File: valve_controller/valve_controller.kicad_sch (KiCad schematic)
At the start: 35 parts, among them J1 643260100604, J10 643260100604, J11 643260100604, J2 T4143512051-000, J3 M12A-04PMMP-SF8001, J4 ESP_PROG, J5 643260100604, J6 643260100604, J7 643260100604, J8 643260100604, J9 643260100604, U1 LAN8720A, U2 ADS1115IDGS, U3 MCP4728, U4 ESP32-WROOM-32, U5 LM2596S-5, U7 ADS1115IDGS, U8 MCP4728, U9 AP2112K-3.3, Y2 ASE-25.000MHZ-LC-T

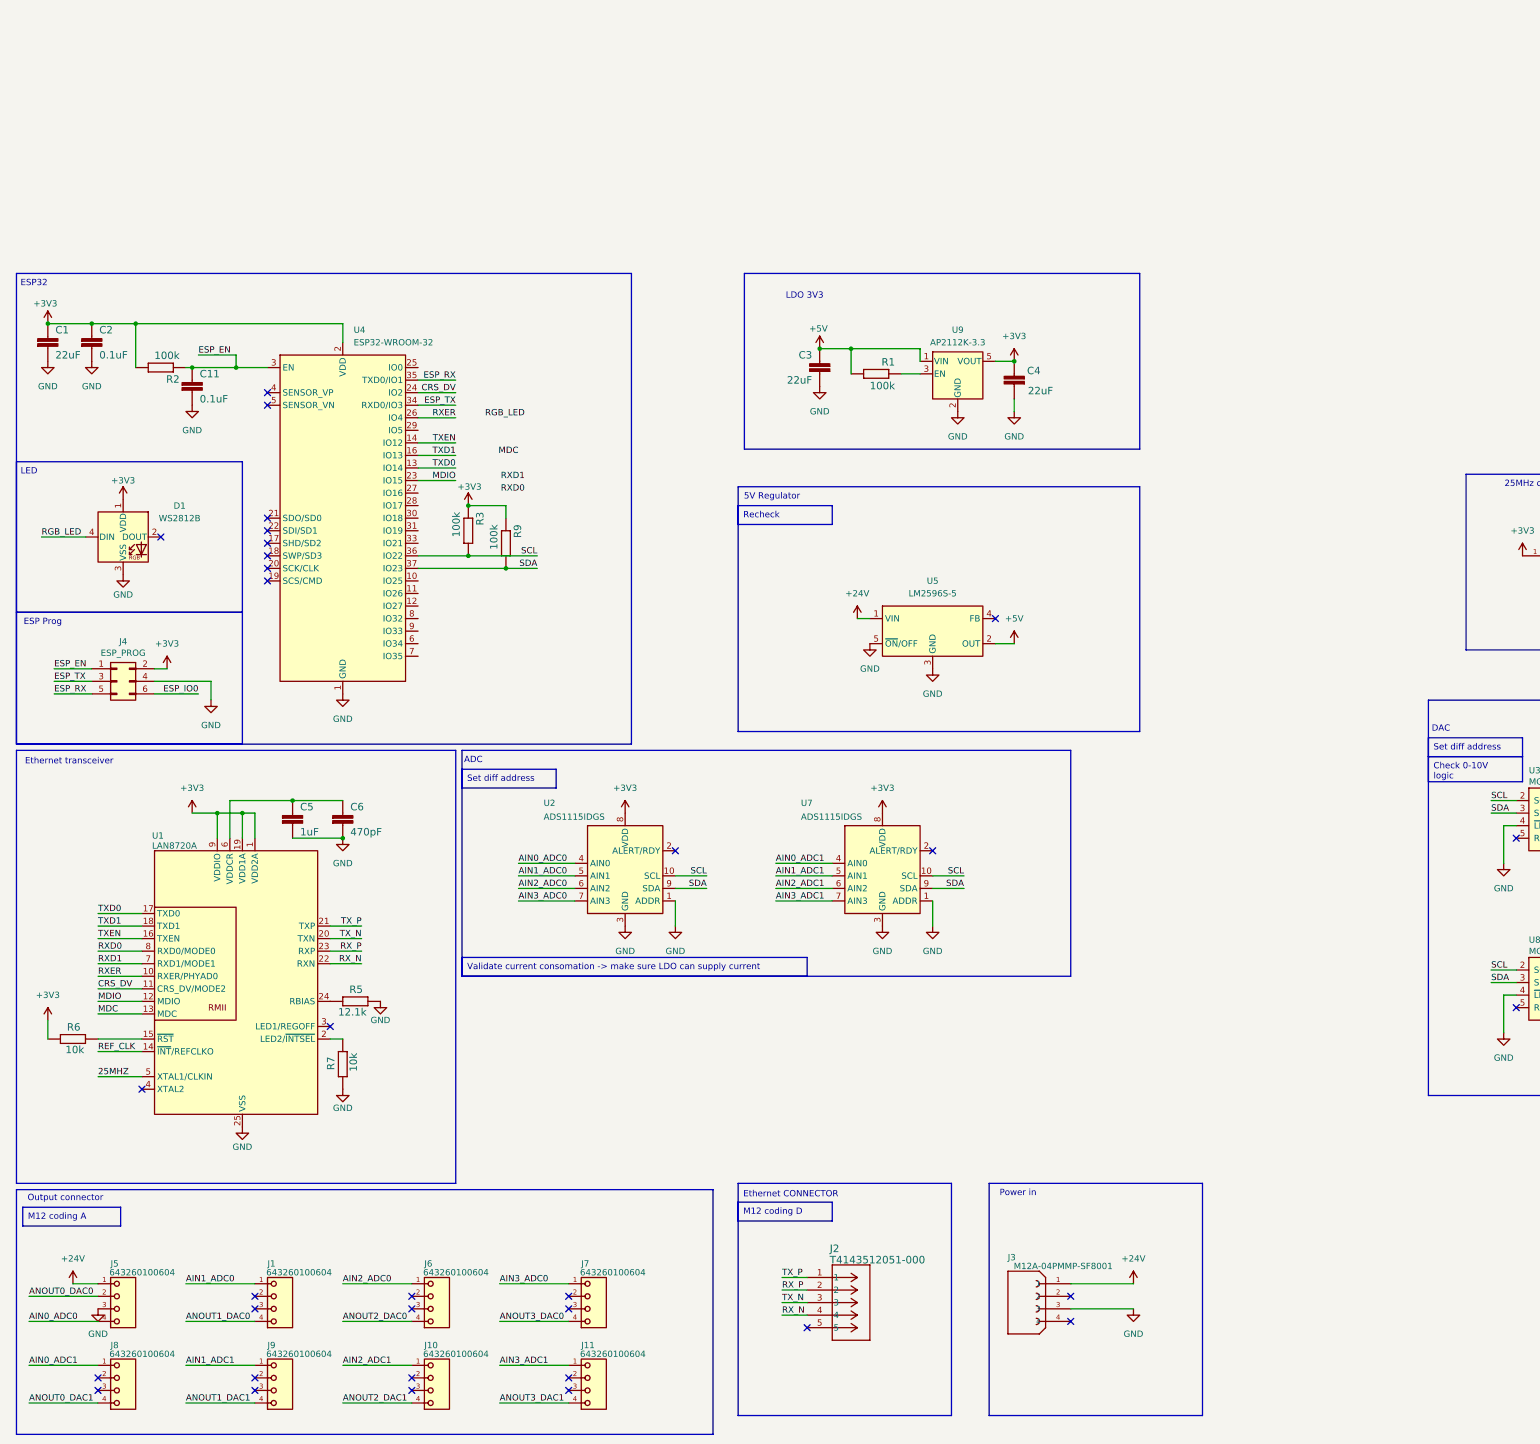
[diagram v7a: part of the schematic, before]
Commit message: new regulator
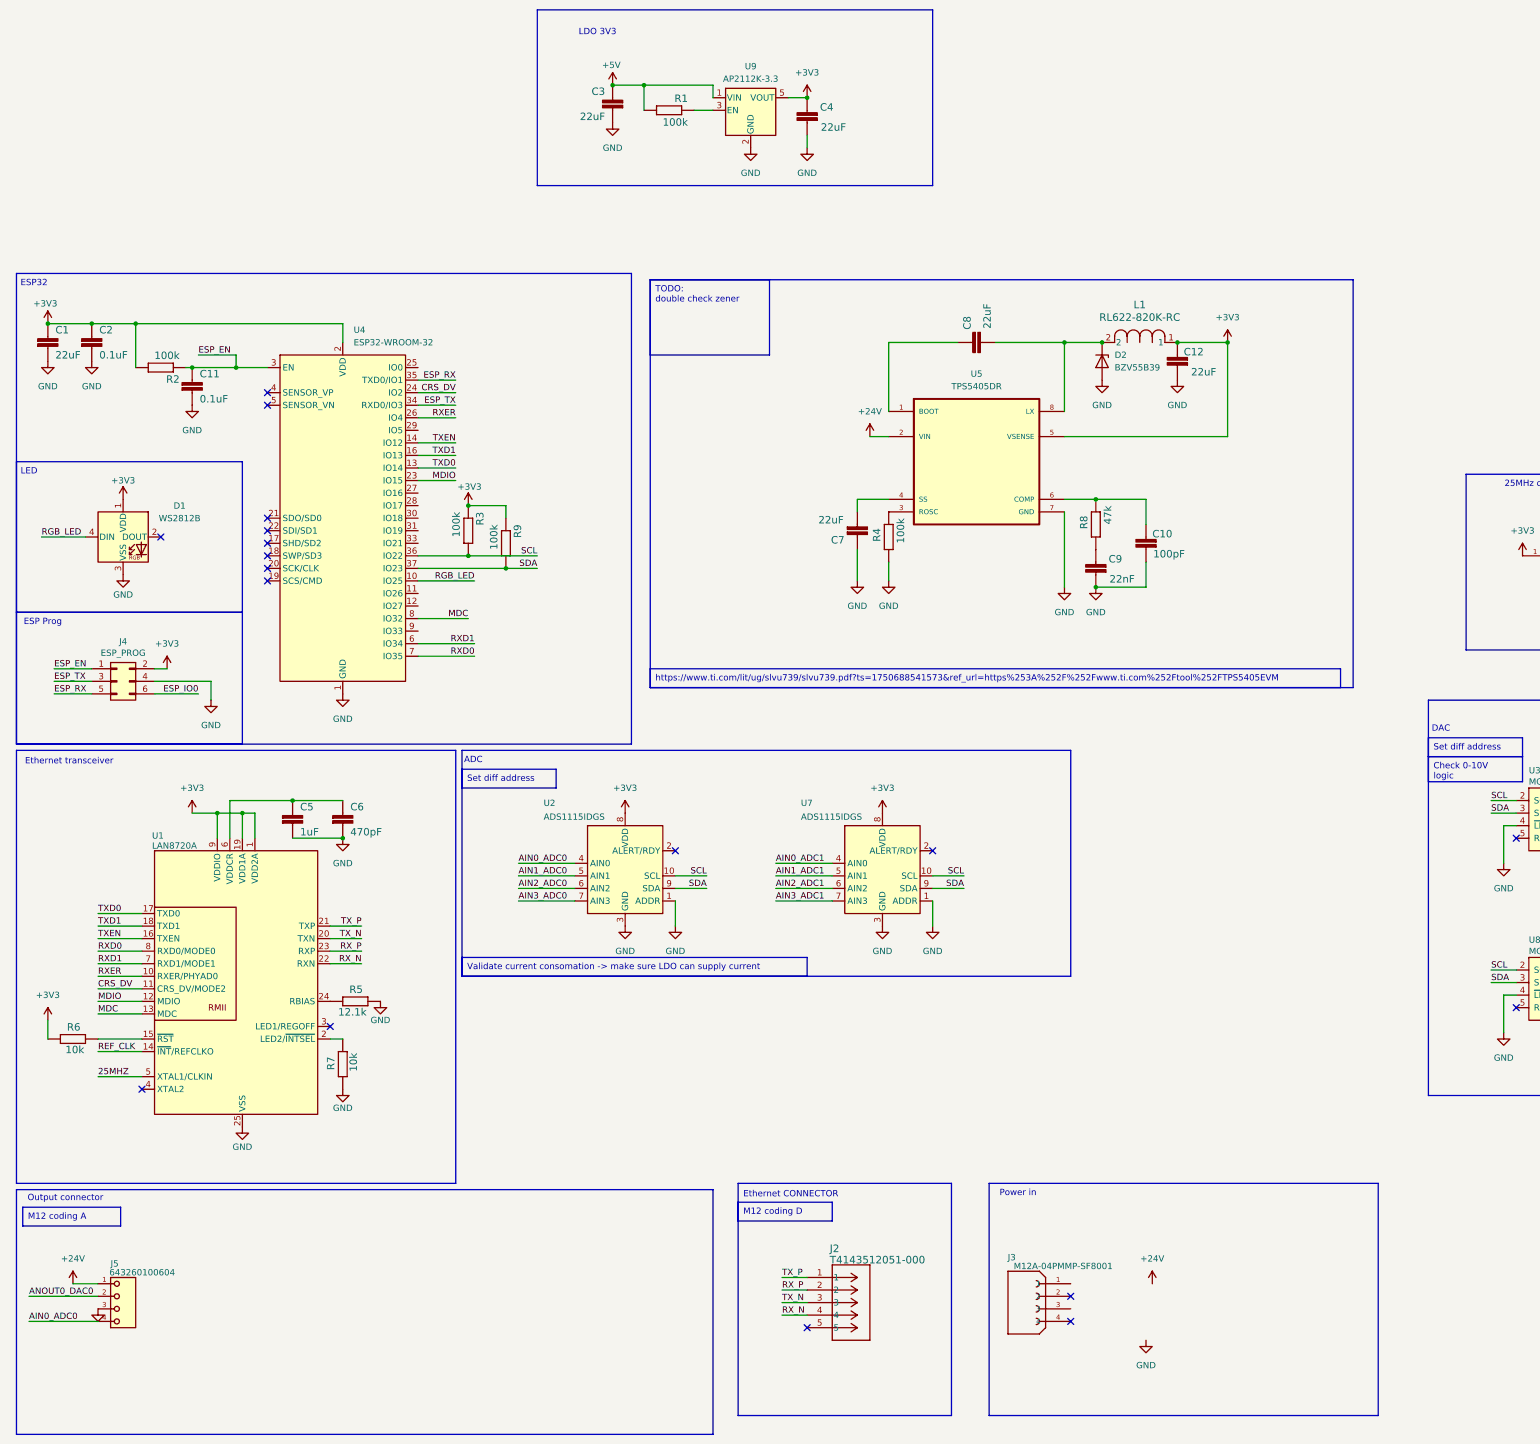
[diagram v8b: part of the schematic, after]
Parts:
- removed J1, J10, J11, J6, J7, J8, J9: 643260100604, 643260100604:643260100604, symbol 643260100604:643260100604
- removed U5: LM2596S-5, Package_TO_SOT_SMD:TO-263-5_TabPin3, symbol Regulator_Switching:LM2596S-5
- added C10: 100pF, Capacitor_SMD:C_0603_1608Metric, symbol SerialChiller-eagle-import:C-EUC1206
- added C12, C7, C8: 22uF, Capacitor_SMD:C_0603_1608Metric, symbol SerialChiller-eagle-import:C-EUC1206
- added C9: 22nF, Capacitor_SMD:C_0603_1608Metric, symbol SerialChiller-eagle-import:C-EUC1206
- added D2: BZV55B39, Diode_SMD:D_MiniMELF, symbol Diode:BZV55B39
- added L1: RL622-820K-RC, RL622_Series, symbol 2025-06-23_19-09-54:RL622-820K-RC
- added R4: 100k, Resistor_SMD:R_0603_1608Metric, symbol SerialChiller-eagle-import:R-EU_R0603
- added R8: 47k, Resistor_SMD:R_0603_1608Metric, symbol SerialChiller-eagle-import:R-EU_R0603
- added U5: TPS5405DR, TPS5405DR:SOIC127P599X175-8N, symbol TPS5405DR:TPS5405DR
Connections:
- net +24V: now also U5.2 (VIN); no longer J3.1
- net +3V3: now also C12.1, L1.1, U5.5 (VSENSE)
- net GND: now also C10.2, C12.2, C7.1, C9.2, D2.2 (A), R4.2, U5.7 (GND); no longer J3.3
- net MDC: now also U4.8 (IO32)
- net RGB_LED: now also U4.10 (IO25)
- net RXD0: now also U4.7 (IO35)
- net RXD1: now also U4.6 (IO34)
- new net: C7.2, U5.4 (SS)
- new net: C8.2, D2.1 (K), L1.2, U5.8 (LX)
- new net: R4.1, U5.3 (ROSC)
- new net: C9.1, R8.2
- new net: C10.1, R8.1, U5.6 (COMP)
- new net: C8.1, U5.1 (BOOT)
- no-connect marks 33 -> 18
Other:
- note removed: "5V Regulator"
- moved on the sheet: C3, C4, R1, U9
